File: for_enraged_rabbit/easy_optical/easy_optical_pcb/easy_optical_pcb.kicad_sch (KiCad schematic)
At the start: 11 parts, among them J1 Conn_01x03, Q1 AO3402_N_Mosfet, U1 ITR20403

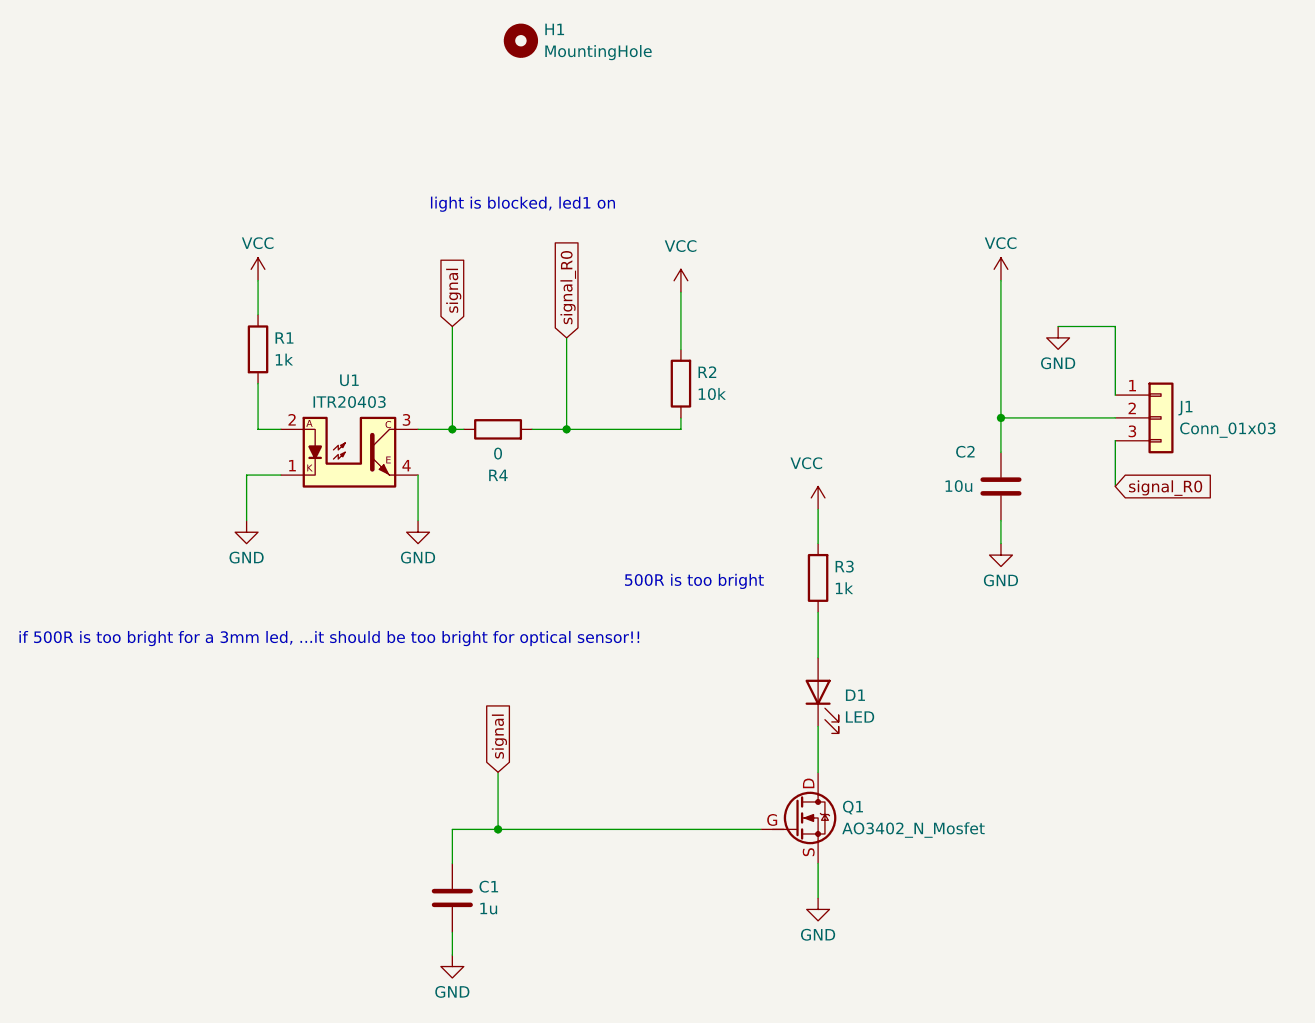
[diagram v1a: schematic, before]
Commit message: add 28mm servo selector Version2
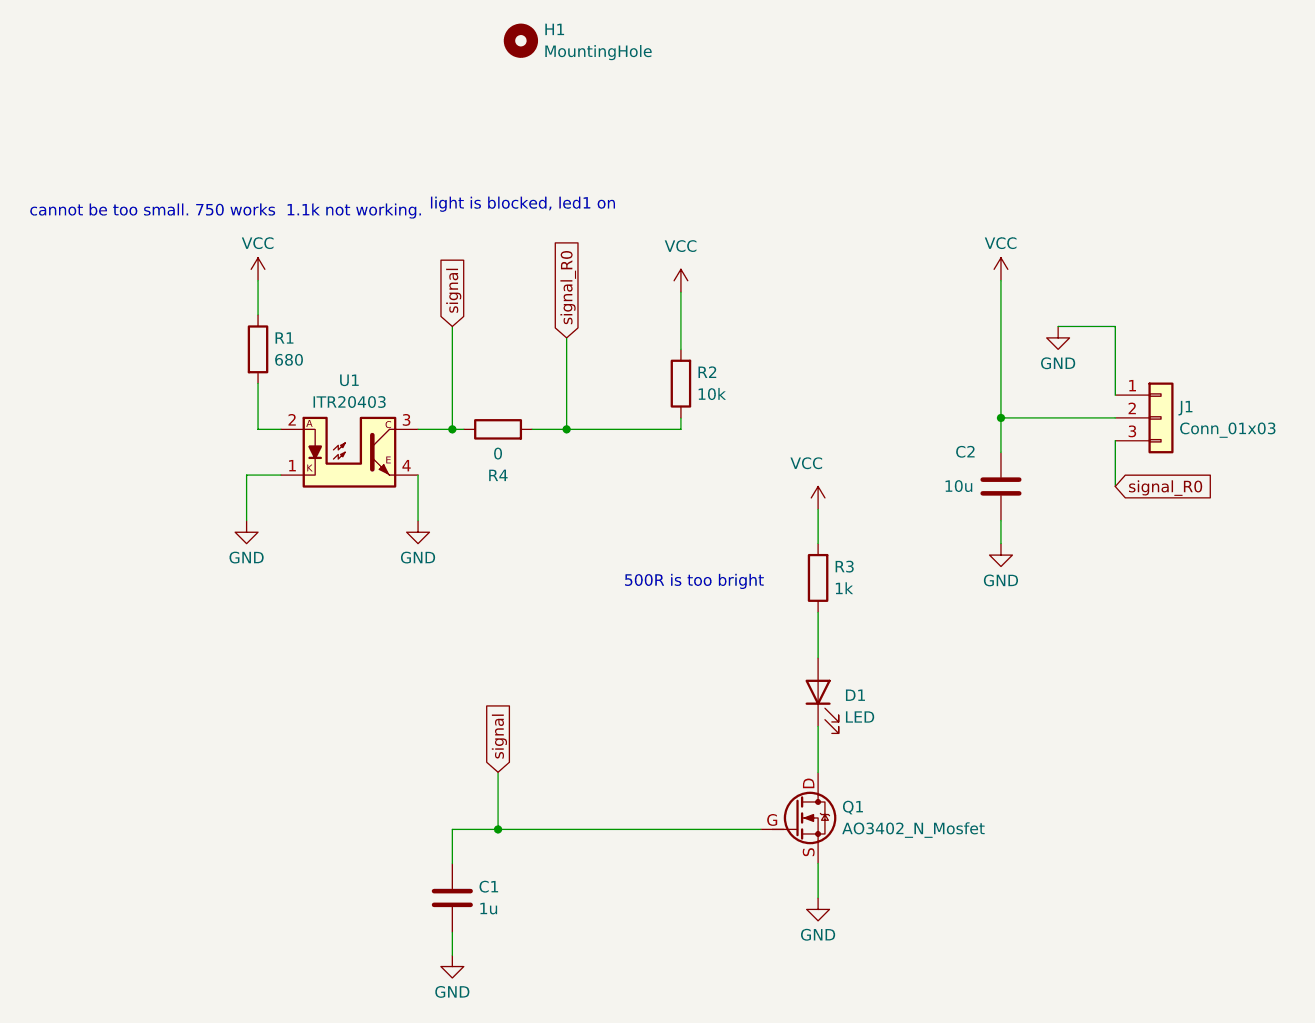
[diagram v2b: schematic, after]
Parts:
- R1: value 1k -> 680
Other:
- note added: "cannot be too small. 750 works 1.1k not working."
- note removed: "if 500R is too bright for a 3mm led, ...it should be too bright for optical sensor!!"
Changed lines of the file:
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@@
 		)
 	)
-	(text "if 500R is too bright for a 3mm led, ...it should be too bright for optical sensor!!"
-		(exclude_from_sim no)
-		(at 71.12 110.49 0)
+	(text "cannot be too small. 750 works  1.1k not working."
+		(exclude_from_sim no)
+		(at 72.39 62.992 0)
 		(effects
 			(font
@@
 			)
 		)
-		(property "Value" "1k"
+		(property "Value" "680"
 			(at 99.568 78.6821 0)
 			(effects
